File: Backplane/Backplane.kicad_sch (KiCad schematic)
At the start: 44 parts, among them J10 Conn_01x02, J11 Conn_01x02, J12 Conn_02x12_Odd_Even, J13 Conn_01x02, J14 Conn_01x02, J15 Conn_01x02, J17 Conn_01x02, J18 Conn_01x02, J19 Conn_01x02_Pin, J20 Conn_01x02_Pin, J21 Conn_01x02_Pin, J22 Conn_01x02_Pin, J23 Conn_01x02_Pin, J24 Conn_01x02_Pin, J25 Conn_01x02_Pin, J26 Conn_01x02_Pin, J27 Conn_01x02, J28 Conn_01x02, J29 Conn_01x02, J30 Conn_01x02, J31 Conn_01x02, J32 Conn_01x02, J33 Conn_01x02, J34 Conn_01x02, J35 Conn_01x02, J36 Conn_01x02, J37 Conn_01x02, J5 Conn_01x02, J6 1720420202, J7 Conn_01x02, J8 Conn_01x02, J9 Conn_01x02

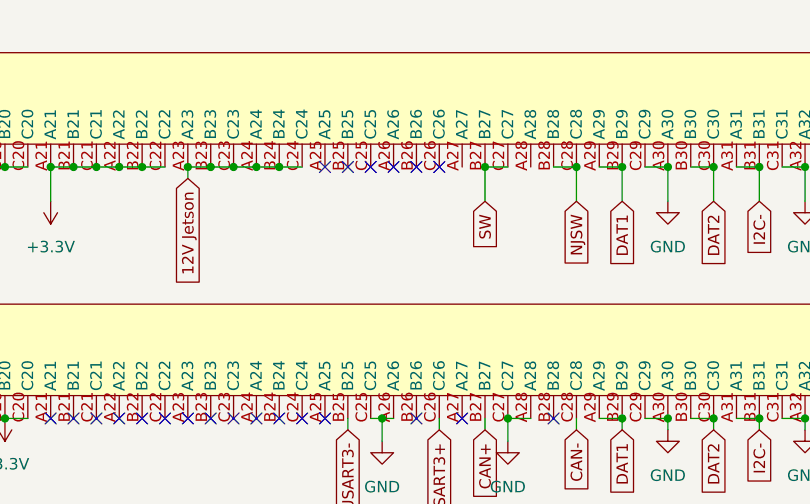
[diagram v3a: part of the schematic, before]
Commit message: Moved I2C Pins for Power Card
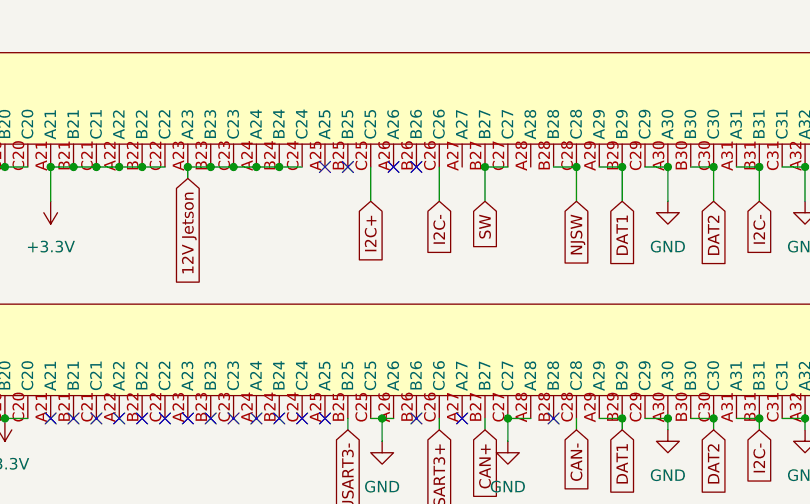
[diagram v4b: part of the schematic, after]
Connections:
- net I2C+: now also J1.C25
- net I2C-: now also J1.C26
- no-connect marks 70 -> 68
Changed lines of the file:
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@@
 	)
 	(no_connect
-		(at 227.33 34.29)
-	)
-	(no_connect
 		(at 179.07 119.38)
 	)
@@
 	)
 	(no_connect
-		(at 219.71 34.29)
-	)
-	(no_connect
 		(at 209.55 62.23)
 	)
@@
 	(wire
 		(pts
+			(xy 227.33 38.1) (xy 227.33 34.29)
+		)
+		(stroke
+			(width 0)
+			(type default)
+		)
+	)
+	(wire
+		(pts
 			(xy 168.91 275.59) (xy 163.83 275.59)
 		)
@@
 	(wire
 		(pts
+			(xy 219.71 38.1) (xy 219.71 34.29)
+		)
+		(stroke
+			(width 0)
+			(type default)
+		)
+	)
+	(wire
+		(pts
 			(xy 330.2 190.5) (xy 331.47 190.5)
 		)
@@
 	(global_label "I2C+"
 		(shape input)
+		(at 219.71 38.1 270)
+		(fields_autoplaced yes)
+		(effects
+			(font
+				(size 1.27 1.27)
+			)
+			(justify right)
+		)
+		(property "Intersheetrefs" "${INTERSHEET_REFS}"
+			(at 219.71 45.7419 90)
+			(effects
+				(font
+					(size 1.27 1.27)
+				)
+				(justify right)
+				(hide yes)
+			)
+		)
+	)
+	(global_label "I2C+"
+		(shape input)
 		(at 273.05 63.5 270)
 		(fields_autoplaced yes)
@@
 			(effects
 				(font
+					(size 1.27 1.27)
+				)
+				(justify right)
+				(hide yes)
+			)
+		)
+	)
+	(global_label "I2C-"
+		(shape input)
+		(at 227.33 38.1 270)
+		(fields_autoplaced yes)
+		(effects
+			(font
+				(size 1.27 1.27)
+			)
+			(justify right)
+		)
+		(property "Intersheetrefs" "${INTERSHEET_REFS}"
+			(at 227.33 45.7419 90)
+			(effects
+				(font
